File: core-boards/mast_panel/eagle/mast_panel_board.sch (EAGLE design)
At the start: 30 parts, among them J1 2-PIN_2MM-V, J4 4-PIN_2MM-H, U1 ATMEGA328P-AUR, U3 MCP2551T-I/SN

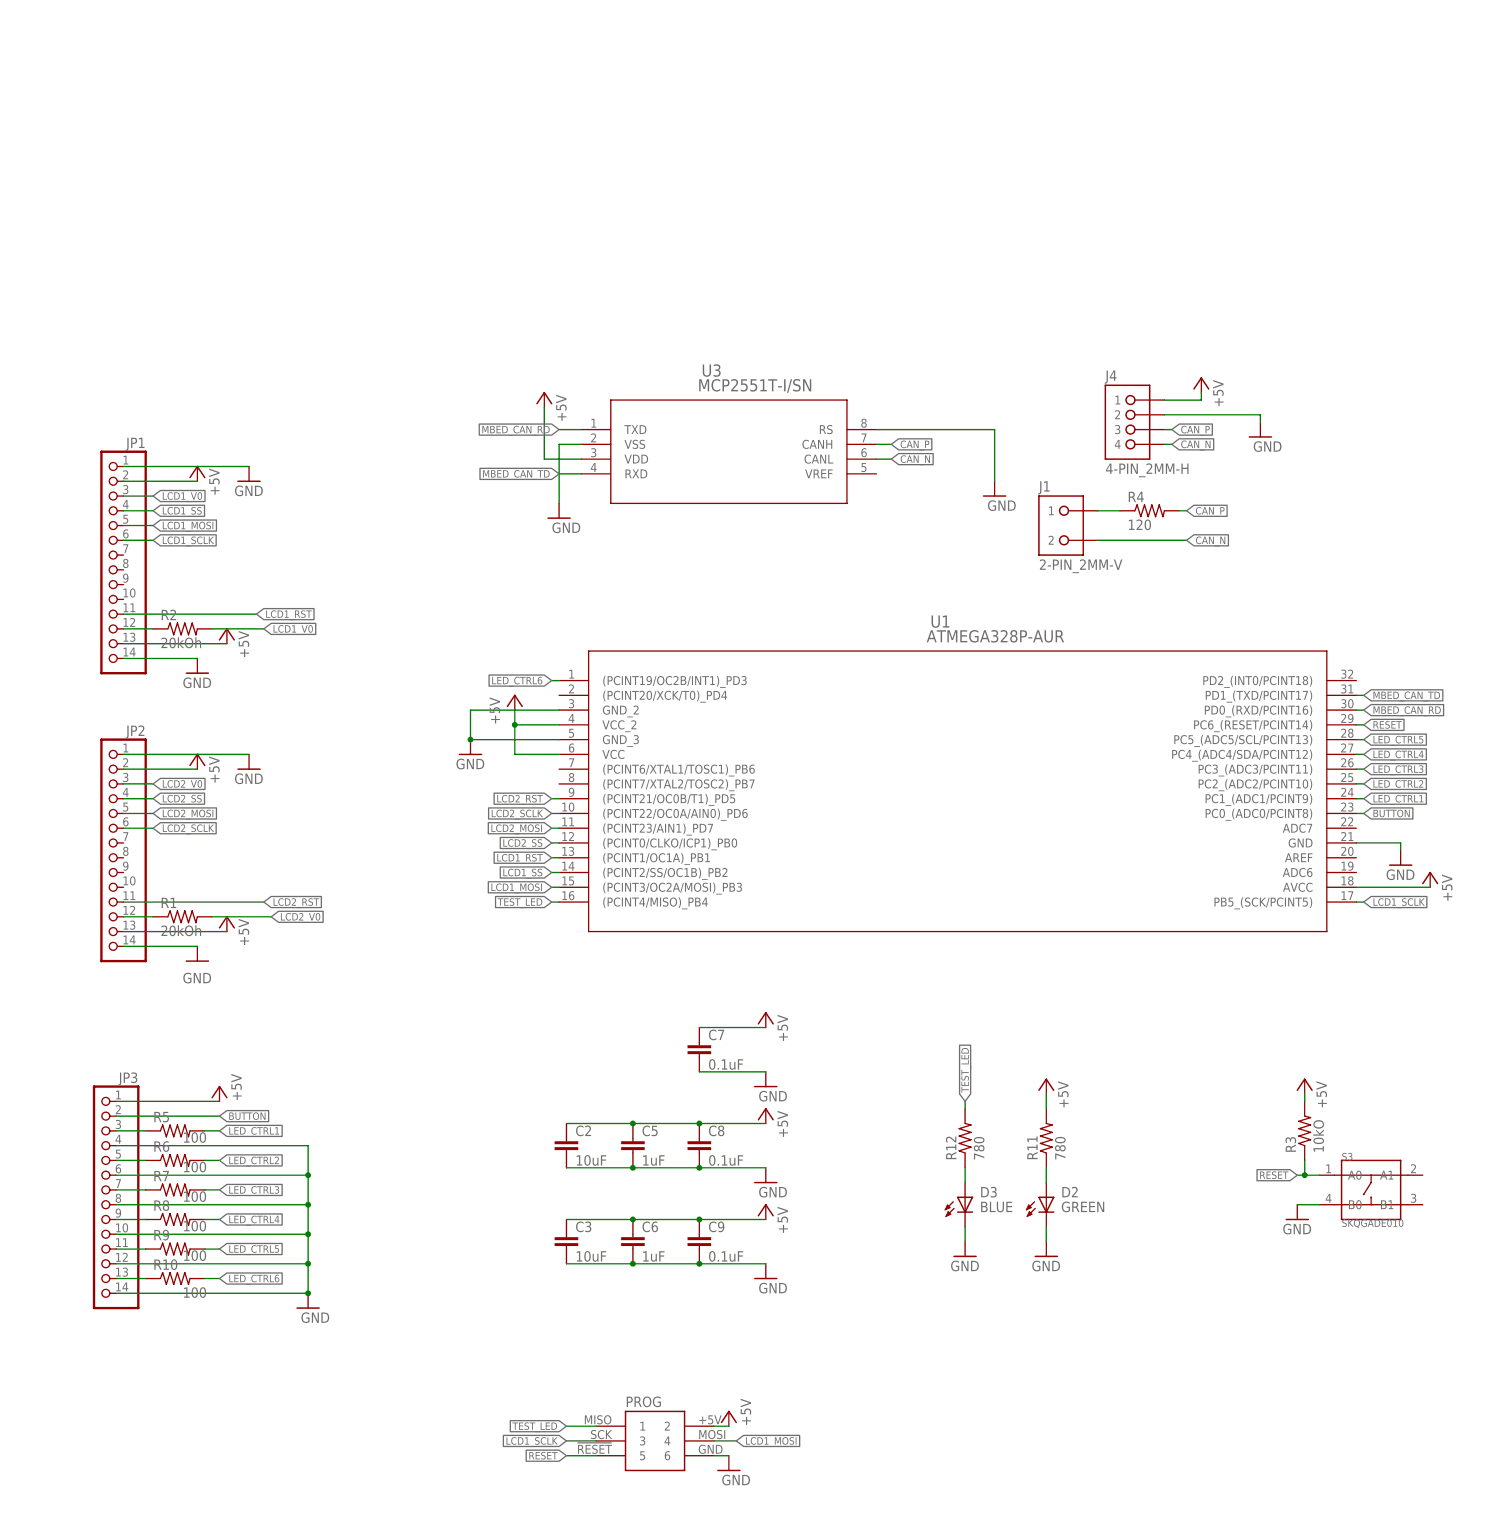
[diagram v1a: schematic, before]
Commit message: 2/23/19
Changed out resistors, fixed SPI connections on board
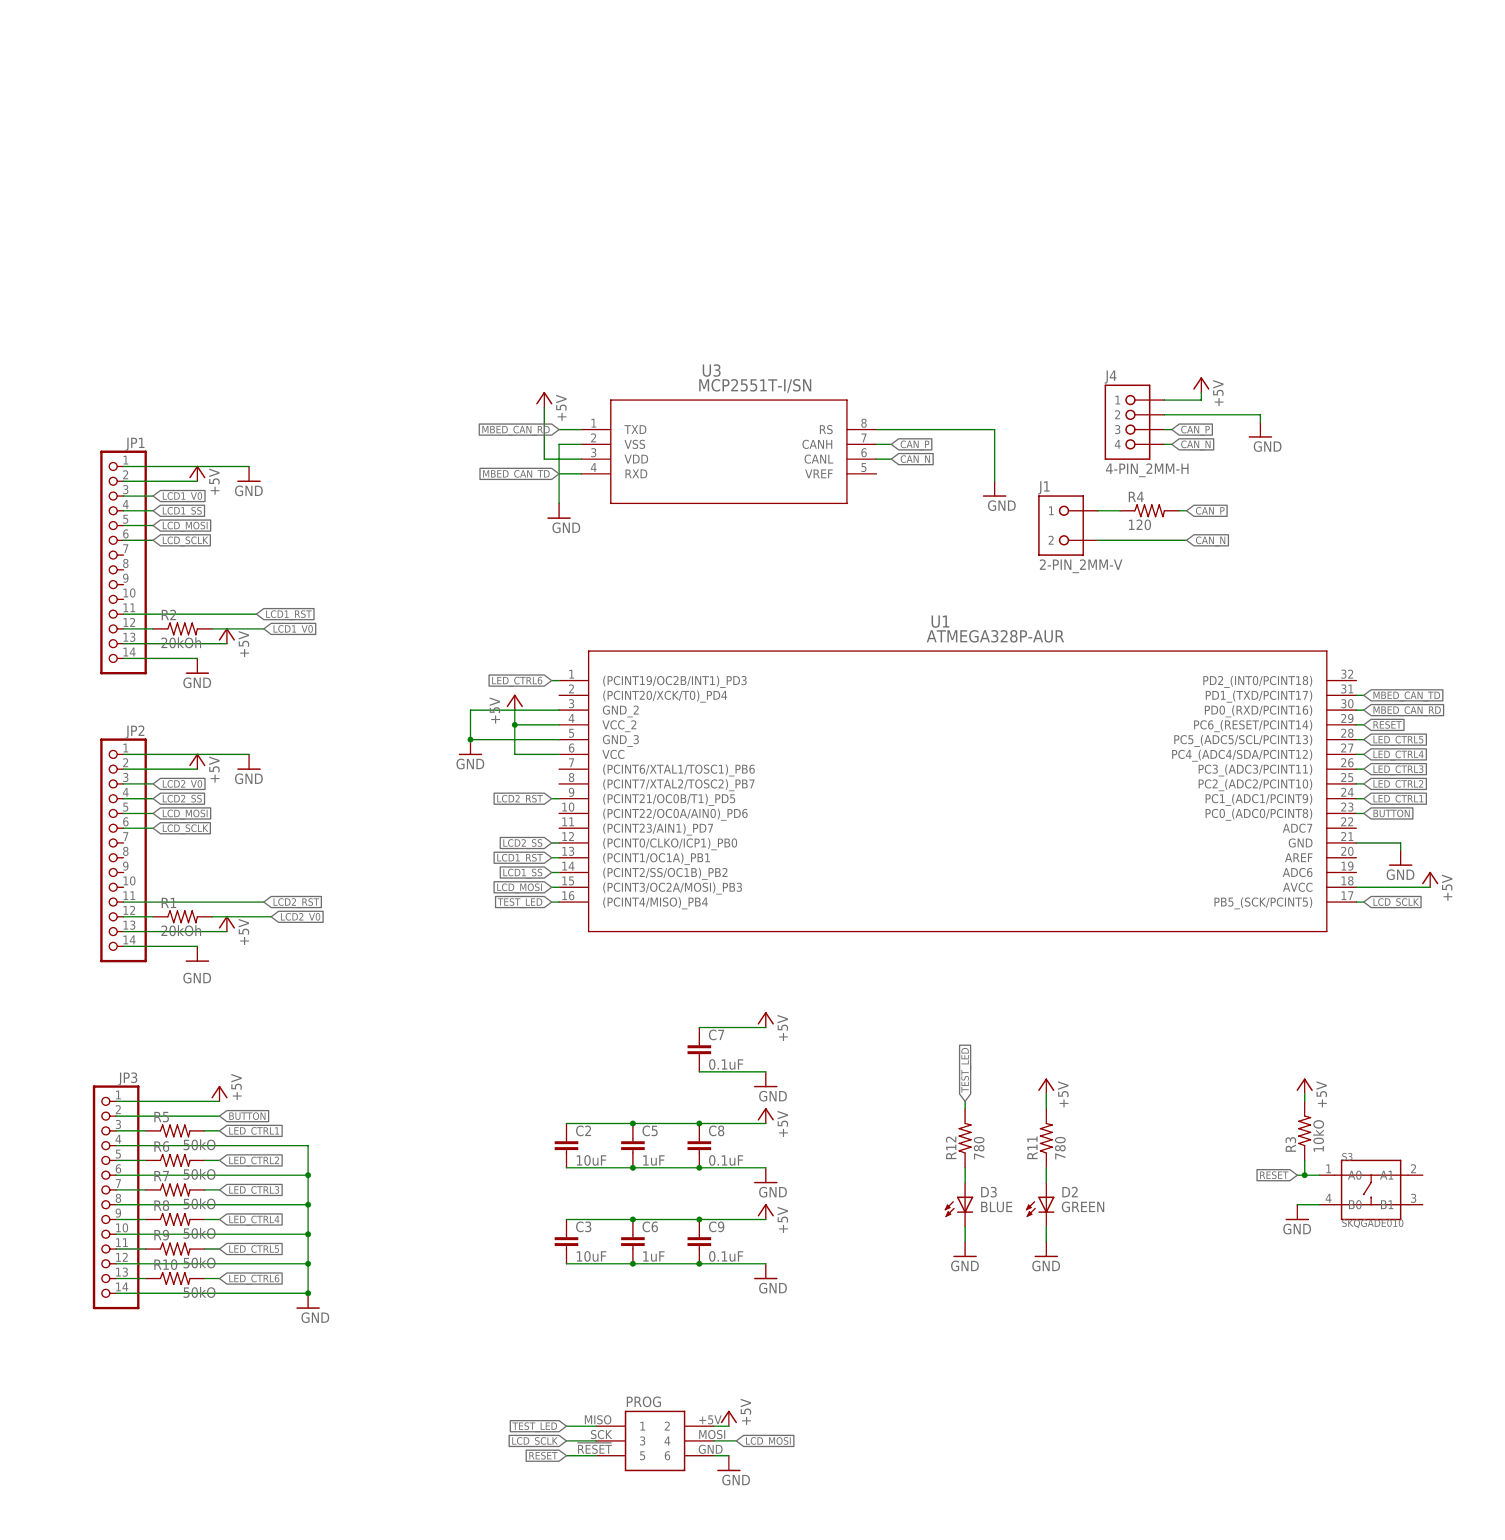
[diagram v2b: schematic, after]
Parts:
- R10, R5, R6, R7, R8, R9: value 100 -> 50kO; device rcl:R-US_R0402 -> rcl:R-US_R0805
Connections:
- removed net LCD1_MOSI: JP1.5, PROG.4, U1.(PCINT3/OC2A/MOSI)_PB3
- removed net LCD1_SCLK: JP1.6, PROG.3, U1.PB5_(SCK/PCINT5)
- removed net LCD2_MOSI: JP2.5, U1.(PCINT23/AIN1)_PD7
- removed net LCD2_SCLK: JP2.6, U1.(PCINT22/OC0A/AIN0)_PD6
- new net LCD_MOSI: JP1.5, JP2.5, PROG.4, U1.(PCINT3/OC2A/MOSI)_PB3
- new net LCD_SCLK: JP1.6, JP2.6, PROG.3, U1.PB5_(SCK/PCINT5)
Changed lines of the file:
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@@
 <part name="R4" library="rcl" library_urn="urn:adsk.eagle:library:334" deviceset="R-US_" device="R0603" package3d_urn="urn:adsk.eagle:package:23555/3" value="120"/>
 <part name="U1" library="MastPanel" deviceset="ATMEGA328P-AUR" device=""/>
-<part name="R5" library="rcl" library_urn="urn:adsk.eagle:library:334" deviceset="R-US_" device="R0402" package3d_urn="urn:adsk.eagle:package:23547/3" value="100"/>
-<part name="R6" library="rcl" library_urn="urn:adsk.eagle:library:334" deviceset="R-US_" device="R0402" package3d_urn="urn:adsk.eagle:package:23547/3" value="100"/>
-<part name="R7" library="rcl" library_urn="urn:adsk.eagle:library:334" deviceset="R-US_" device="R0402" package3d_urn="urn:adsk.eagle:package:23547/3" value="100"/>
-<part name="R8" library="rcl" library_urn="urn:adsk.eagle:library:334" deviceset="R-US_" device="R0402" package3d_urn="urn:adsk.eagle:package:23547/3" value="100"/>
-<part name="R9" library="rcl" library_urn="urn:adsk.eagle:library:334" deviceset="R-US_" device="R0402" package3d_urn="urn:adsk.eagle:package:23547/3" value="100"/>
-<part name="R10" library="rcl" library_urn="urn:adsk.eagle:library:334" deviceset="R-US_" device="R0402" package3d_urn="urn:adsk.eagle:package:23547/3" value="100"/>
 <part name="JP1" library="pinhead" library_urn="urn:adsk.eagle:library:325" deviceset="PINHD-1X14" device="" package3d_urn="urn:adsk.eagle:package:22417/2"/>
 <part name="JP2" library="pinhead" library_urn="urn:adsk.eagle:library:325" deviceset="PINHD-1X14" device="" package3d_urn="urn:adsk.eagle:package:22417/2"/>
@@
 <part name="R3" library="rcl" library_urn="urn:adsk.eagle:library:334" deviceset="R-US_" device="R0603" package3d_urn="urn:adsk.eagle:package:23555/3" value="10kO"/>
 <part name="P+12" library="supply1" library_urn="urn:adsk.eagle:library:371" deviceset="+5V" device=""/>
+<part name="R5" library="rcl" library_urn="urn:adsk.eagle:library:334" deviceset="R-US_" device="R0805" package3d_urn="urn:adsk.eagle:package:23553/2" value="50kO"/>
+<part name="R6" library="rcl" library_urn="urn:adsk.eagle:library:334" deviceset="R-US_" device="R0805" package3d_urn="urn:adsk.eagle:package:23553/2" value="50kO"/>
+<part name="R7" library="rcl" library_urn="urn:adsk.eagle:library:334" deviceset="R-US_" device="R0805" package3d_urn="urn:adsk.eagle:package:23553/2" value="50kO"/>
+<part name="R8" library="rcl" library_urn="urn:adsk.eagle:library:334" deviceset="R-US_" device="R0805" package3d_urn="urn:adsk.eagle:package:23553/2" value="50kO"/>
+<part name="R9" library="rcl" library_urn="urn:adsk.eagle:library:334" deviceset="R-US_" device="R0805" package3d_urn="urn:adsk.eagle:package:23553/2" value="50kO"/>
+<part name="R10" library="rcl" library_urn="urn:adsk.eagle:library:334" deviceset="R-US_" device="R0805" package3d_urn="urn:adsk.eagle:package:23553/2" value="50kO"/>
 </parts>
 <sheets>
@@
 <attribute name="VALUE" x="83.5406" y="6.5786" size="2.0828" layer="96" ratio="6" rot="SR0"/>
 </instance>
-<instance part="R5" gate="G$1" x="-45.72" y="-77.47" smashed="yes">
-<attribute name="NAME" x="-49.53" y="-75.9714" size="1.778" layer="95"/>
-<attribute name="VALUE" x="-44.45" y="-79.502" size="1.778" layer="96"/>
-</instance>
-<instance part="R6" gate="G$1" x="-45.72" y="-82.55" smashed="yes">
-<attribute name="NAME" x="-49.53" y="-81.0514" size="1.778" layer="95"/>
-<attribute name="VALUE" x="-44.45" y="-84.582" size="1.778" layer="96"/>
-</instance>
-<instance part="R7" gate="G$1" x="-45.72" y="-87.63" smashed="yes">
-<attribute name="NAME" x="-49.53" y="-86.1314" size="1.778" layer="95"/>
-<attribute name="VALUE" x="-44.45" y="-89.662" size="1.778" layer="96"/>
-</instance>
-<instance part="R8" gate="G$1" x="-45.72" y="-92.71" smashed="yes">
-<attribute name="NAME" x="-49.53" y="-91.2114" size="1.778" layer="95"/>
-<attribute name="VALUE" x="-44.45" y="-94.742" size="1.778" layer="96"/>
-</instance>
-<instance part="R9" gate="G$1" x="-45.72" y="-97.79" smashed="yes">
-<attribute name="NAME" x="-49.53" y="-96.2914" size="1.778" layer="95"/>
-<attribute name="VALUE" x="-44.45" y="-99.822" size="1.778" layer="96"/>
-</instance>
-<instance part="R10" gate="G$1" x="-45.72" y="-102.87" smashed="yes">
-<attribute name="NAME" x="-49.53" y="-101.3714" size="1.778" layer="95"/>
-<attribute name="VALUE" x="-44.45" y="-106.172" size="1.778" layer="96"/>
-</instance>
 <instance part="JP1" gate="A" x="-57.15" y="21.59" smashed="yes" rot="MR0">
 <attribute name="NAME" x="-50.8" y="40.005" size="1.778" layer="95" rot="MR0"/>
@@
 <instance part="P+12" gate="1" x="148.59" y="-68.58" smashed="yes">
 <attribute name="VALUE" x="152.4" y="-73.66" size="1.778" layer="96" rot="R90"/>
+</instance>
+<instance part="R5" gate="G$1" x="-45.72" y="-77.47" smashed="yes">
+<attribute name="NAME" x="-49.53" y="-75.9714" size="1.778" layer="95"/>
+<attribute name="VALUE" x="-44.45" y="-80.772" size="1.778" layer="96"/>
+</instance>
+<instance part="R6" gate="G$1" x="-45.72" y="-82.55" smashed="yes">
+<attribute name="NAME" x="-49.53" y="-81.0514" size="1.778" layer="95"/>
+<attribute name="VALUE" x="-44.45" y="-85.852" size="1.778" layer="96"/>
+</instance>
+<instance part="R7" gate="G$1" x="-45.72" y="-87.63" smashed="yes">
+<attribute name="NAME" x="-49.53" y="-86.1314" size="1.778" layer="95"/>
+<attribute name="VALUE" x="-44.45" y="-90.932" size="1.778" layer="96"/>
+</instance>
+<instance part="R8" gate="G$1" x="-45.72" y="-92.71" smashed="yes">
+<attribute name="NAME" x="-49.53" y="-91.2114" size="1.778" layer="95"/>
+<attribute name="VALUE" x="-44.45" y="-96.012" size="1.778" layer="96"/>
+</instance>
+<instance part="R9" gate="G$1" x="-45.72" y="-97.79" smashed="yes">
+<attribute name="NAME" x="-49.53" y="-96.2914" size="1.778" layer="95"/>
+<attribute name="VALUE" x="-44.45" y="-101.092" size="1.778" layer="96"/>
+</instance>
+<instance part="R10" gate="G$1" x="-45.72" y="-102.87" smashed="yes">
+<attribute name="NAME" x="-49.53" y="-101.3714" size="1.778" layer="95"/>
+<attribute name="VALUE" x="-44.45" y="-106.172" size="1.778" layer="96"/>
 </instance>
 </instances>
@@
 <segment>
 <wire x1="-55.88" y1="-77.47" x2="-50.8" y2="-77.47" width="0.1524" layer="91"/>
+<pinref part="JP3" gate="A" pin="3"/>
 <pinref part="R5" gate="G$1" pin="1"/>
-<pinref part="JP3" gate="A" pin="3"/>
 </segment>
 </net>
@@
 <segment>
 <wire x1="-55.88" y1="-87.63" x2="-50.8" y2="-87.63" width="0.1524" layer="91"/>
+<pinref part="JP3" gate="A" pin="7"/>
 <pinref part="R7" gate="G$1" pin="1"/>
-<pinref part="JP3" gate="A" pin="7"/>
 </segment>
 </net>
@@
 <segment>
 <wire x1="-55.88" y1="-92.71" x2="-50.8" y2="-92.71" width="0.1524" layer="91"/>
+<pinref part="JP3" gate="A" pin="9"/>
 <pinref part="R8" gate="G$1" pin="1"/>
-<pinref part="JP3" gate="A" pin="9"/>
 </segment>
 </net>
@@
 <segment>
 <wire x1="-55.88" y1="-97.79" x2="-50.8" y2="-97.79" width="0.1524" layer="91"/>
+<pinref part="JP3" gate="A" pin="11"/>
 <pinref part="R9" gate="G$1" pin="1"/>
-<pinref part="JP3" gate="A" pin="11"/>
 </segment>
 </net>
@@
 <segment>
 <wire x1="-55.88" y1="-102.87" x2="-50.8" y2="-102.87" width="0.1524" layer="91"/>
+<pinref part="JP3" gate="A" pin="13"/>
 <pinref part="R10" gate="G$1" pin="1"/>
-<pinref part="JP3" gate="A" pin="13"/>
 </segment>
 </net>
@@
 <segment>
 <wire x1="-55.88" y1="-82.55" x2="-50.8" y2="-82.55" width="0.1524" layer="91"/>
+<pinref part="JP3" gate="A" pin="5"/>
 <pinref part="R6" gate="G$1" pin="1"/>
-<pinref part="JP3" gate="A" pin="5"/>
 </segment>
 </net>
@@
 </segment>
 </net>
-<net name="LCD1_SCLK" class="0">
+<net name="LCD_SCLK" class="0">
 <segment>
 <label x="-49.53" y="24.13" size="1.27" layer="95" xref="yes"/>
@@
 <label x="21.59" y="-130.81" size="1.27" layer="95" rot="R180" xref="yes"/>
 </segment>
-</net>
-<net name="LCD2_SCLK" class="0">
 <segment>
 <label x="-49.53" y="-25.4" size="1.27" layer="95" xref="yes"/>
@@
 <pinref part="JP2" gate="A" pin="6"/>
 </segment>
-<segment>
-<pinref part="U1" gate="A" pin="(PCINT22/OC0A/AIN0)_PD6"/>
-<wire x1="20.32" y1="-22.86" x2="19.05" y2="-22.86" width="0.1524" layer="91"/>
-<label x="19.05" y="-22.86" size="1.27" layer="95" rot="R180" xref="yes"/>
-</segment>
-</net>
-<net name="LCD1_MOSI" class="0">
+</net>
+<net name="LCD_MOSI" class="0">
 <segment>
 <label x="-49.53" y="26.67" size="1.27" layer="95" xref="yes"/>
@@
 <label x="50.8" y="-130.81" size="1.27" layer="95" xref="yes"/>
 </segment>
+<segment>
+<label x="-49.53" y="-22.86" size="1.27" layer="95" xref="yes"/>
+<wire x1="-49.53" y1="-22.86" x2="-54.61" y2="-22.86" width="0.1524" layer="91"/>
+<pinref part="JP2" gate="A" pin="5"/>
+</segment>
 </net>
 <net name="LCD1_SS" class="0">
@@
 </segment>
 </net>
-<net name="LCD2_MOSI" class="0">
-<segment>
-<label x="-49.53" y="-22.86" size="1.27" layer="95" xref="yes"/>
-<wire x1="-49.53" y1="-22.86" x2="-54.61" y2="-22.86" width="0.1524" layer="91"/>
-<pinref part="JP2" gate="A" pin="5"/>
-</segment>
-<segment>
-<pinref part="U1" gate="A" pin="(PCINT23/AIN1)_PD7"/>
-<wire x1="20.32" y1="-25.4" x2="19.05" y2="-25.4" width="0.1524" layer="91"/>
-<label x="19.05" y="-25.4" size="1.27" layer="95" rot="R180" xref="yes"/>
-</segment>
-</net>
